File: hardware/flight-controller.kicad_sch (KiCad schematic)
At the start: 106 parts, among them J1 USB_C_Receptacle_USB2.0_16P, J10 Screw_Terminal_01x02, J11 Micro_SD_Card_Det_Hirose_DM3AT, J12 Conn_01x03, J13 Conn_01x03, J14 Conn_01x03, J15 Conn_01x03, J16 Screw_Terminal_01x02, J17 Conn_01x04, J18 Screw_Terminal_01x02, J2 Conn_01x02, J3 Conn_Coaxial, J4 Conn_01x04, J5 Screw_Terminal_01x02, J6 Conn_01x04, J7 Screw_Terminal_01x02, J8 Conn_01x04, J9 Screw_Terminal_01x02, U1 BMP384, U2 LSM6DSOTR, U3 MMC5983MA, U4 NEO-M9N, U5 TPS2121RUXR, U6 AP62300TWU, U7 STM32H723VGTx, Y1 Q13FC13500004, Y2 X322525MOB4SI

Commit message: routing pcb
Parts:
- added J19: Conn_01x02, Connector_PinHeader_2.54mm:PinHeader_1x02_P2.54mm_Vertical, symbol Connector_Generic:Conn_01x02
- BZ1: footprint Buzzer_Beeper:Buzzer_12x9.5RM7.6 -> Flight-Controller_Imports:SPKR_PKMCS0909E4000-R1
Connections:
- net BUZZER: now also U7.77 (PA15(JTDI))
- net SWDCLK: now also J19.2 (Pin_2)
- net SWDIO: now also J19.1 (Pin_1)
- no-connect marks 55 -> 54
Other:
- moved on the sheet: D2, D3, D4, R13, R14, R15

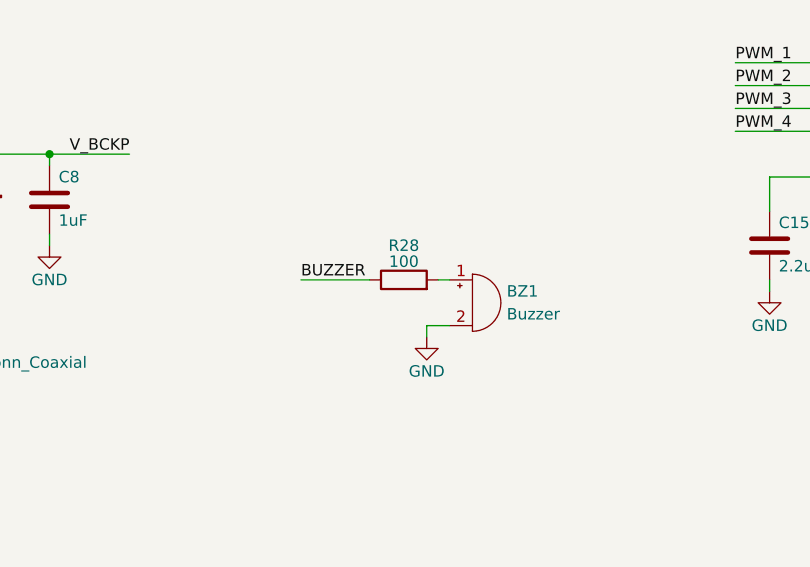
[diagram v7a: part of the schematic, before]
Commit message: added buzzer type
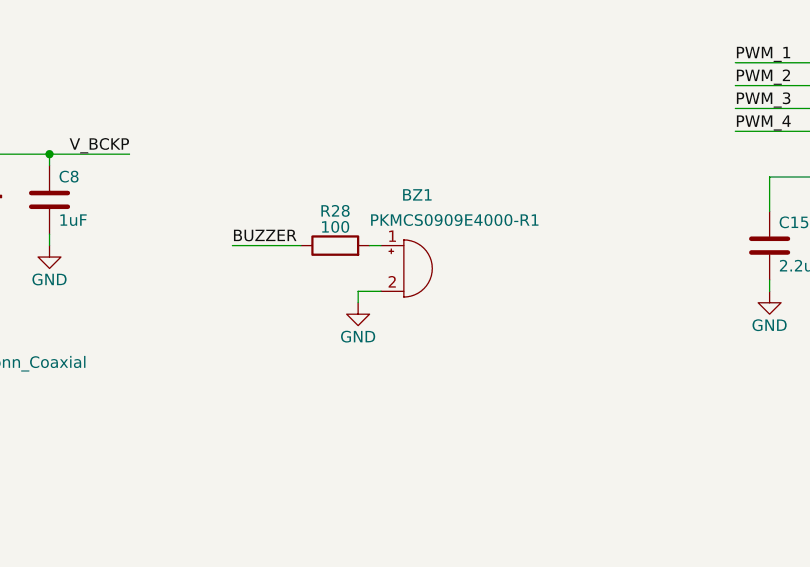
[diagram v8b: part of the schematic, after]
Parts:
- BZ1: value Buzzer -> PKMCS0909E4000-R1
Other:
- moved on the sheet: BZ1, R28
